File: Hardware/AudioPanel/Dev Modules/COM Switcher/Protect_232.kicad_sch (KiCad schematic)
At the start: 52 parts, among them J201 DE9_Socket_MountingHoles, J202 JST-PH UART/I2C, J203 JST-PH UART/I2C

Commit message: Small tweaks
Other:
- company: (none) -> Thomas Francois - KX∅STL
- title: (none) -> COM Port Switcher - COM Port Protection & Level Shift
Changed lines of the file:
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@@
 	(generator_version "9.0")
 	(paper "B")
+	(title_block
+		(title "COM Port Switcher - COM Port Protection & Level Shift")
+		(date "2025-07-26")
+		(rev "A")
+		(company "Thomas Francois - KX∅STL")
+	)
 	(text "RXD: Serial Data from Transceiver to Computer\n~{CTS}: Used by Transceiver to inhibit Computer from transitting serial data\nTXD: Serial Data from Computer to Transceiver\n~{RTS}: Used by Computer to inhibit Transceiver from transmitting serial data\n"
 		(exclude_from_sim no)

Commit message: Added level shifters for all SAMD21s
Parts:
- renumbered C203 to C201, C204 to C202, C208 to C203, C209 to C204, C206 to C205, C210 to C206, C201 to C207, C202 to C208, C205 to C209, C207 to C210, D204 to D201, D201 to D202, D202 to D203, D203 to D204, J203 to J201, J201 to J203, TP211 to TP202, TP202 to TP203, TP212 to TP204, TP203 to TP205, TP213 to TP206, TP204 to TP207, TP214 to TP208, TP205 to TP209, TP215 to TP210, TP206 to TP211, TP207 to TP212, TP208 to TP213, TP209 to TP214, TP210 to TP215

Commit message: Changed DB9 connectors to stacked
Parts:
- J201: renamed from J203; footprint Connector_Dsub:DSUB-9_Male_Horizontal_P2.77x2.84mm_EdgePinOffset7.70mm_Housed_MountingHolesOffset9.12mm -> Libraries:NORCOMP_189-009-513R571; symbol Connector:DE9_Socket_MountingHoles -> library_symbols:DE9_Socket_2X_Stacked; DigiKey (none) -> https://www.digikey.com/en/products/detail/norcomp-inc/189-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
- renumbered C207 to C201, C208 to C202, C201 to C203, C202 to C204, C209 to C205, C205 to C206, C210 to C207, C203 to C208, C204 to C209, C206 to C210, J201 to J203, TP203 to TP202, TP205 to TP203, TP207 to TP204, TP209 to TP205, TP211 to TP206, TP212 to TP207, TP213 to TP208, TP214 to TP209, TP215 to TP210, TP202 to TP211, TP204 to TP212, TP206 to TP213, TP208 to TP214, TP210 to TP215
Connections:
- net CTS_T: now also J201.A8; no longer J201.8
- net DCD_T: now also J201.A1; no longer J201.1
- net DSR_T: now also J201.A6; no longer J201.6
- net DTR_T: now also J201.A4; no longer J201.4
- net GND_232_FROM_RADIO: now also J201.SH1 (PAD), J201.SH2 (PAD); no longer J201.0 (PAD)
- net GND_T: now also J201.A5; no longer J201.5
- net RI_T: now also J201.A9; no longer J201.9
- net RTS_T: now also J201.A7; no longer J201.7
- net RXD_T: now also J201.A2; no longer J201.2
- net TXD_T: now also J201.A3; no longer J201.3
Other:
- moved on the sheet: J201A

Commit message: Fixed I2C pullups to 3V3
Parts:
- renumbered C203 to C201, C204 to C202, C208 to C203, C209 to C204, C206 to C205, C210 to C206, C201 to C207, C202 to C208, C205 to C209, C207 to C210, J203 to J201, J201 to J203, TP211 to TP202, TP202 to TP203, TP212 to TP204, TP203 to TP205, TP213 to TP206, TP204 to TP207, TP214 to TP208, TP205 to TP209, TP215 to TP210, TP206 to TP211, TP207 to TP212, TP208 to TP213, TP209 to TP214, TP210 to TP215
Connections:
- net CTS_232_FROM_RADIO_T renamed CTS_232_FROM_RADIO_3V3
- net CTS_T renamed CTS_3V3
- net CTS_TTL_OUT renamed CTS_3V3TL_OUT
- net DCD_T renamed DCD_3V3
- net DSR_T renamed DSR_3V3
- net DTR_T renamed DTR_3V3
- net GND_T renamed GND_3V3
- net RI_T renamed RI_3V3
- net RTS_232_TO_RADIO renamed RTS_232_3V3O_RADIO
- net RTS_232_TO_RADIO_T renamed RTS_232_3V3O_RADIO_3V3
- net RTS_T renamed RTS_3V3
- net RTS_TTL_IN renamed RTS_3V3TL_IN
- net RXD_232_FROM_RADIO_T renamed RXD_232_FROM_RADIO_3V3
- net RXD_T renamed RXD_3V3
- net RXD_TTL_OUT renamed RXD_3V3TL_OUT
- net TXD_232_TO_RADIO renamed TXD_232_3V3O_RADIO
- net TXD_232_TO_RADIO_T renamed TXD_232_3V3O_RADIO_3V3
- net TXD_T renamed TXD_3V3
- net TXD_TTL_IN renamed TXD_3V3TL_IN

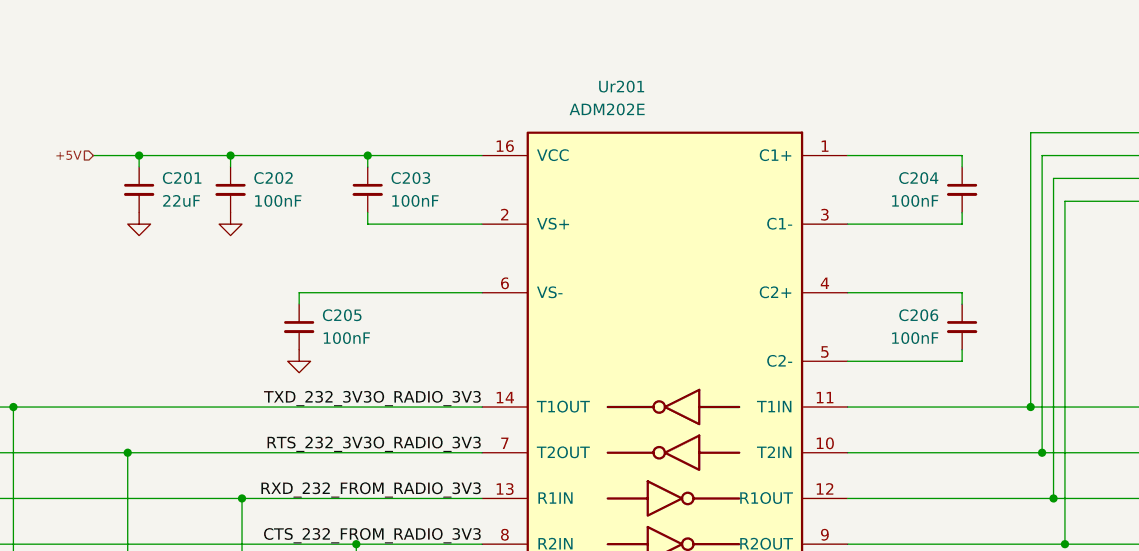
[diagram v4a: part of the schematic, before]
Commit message: Changed passives to Worthington footprints
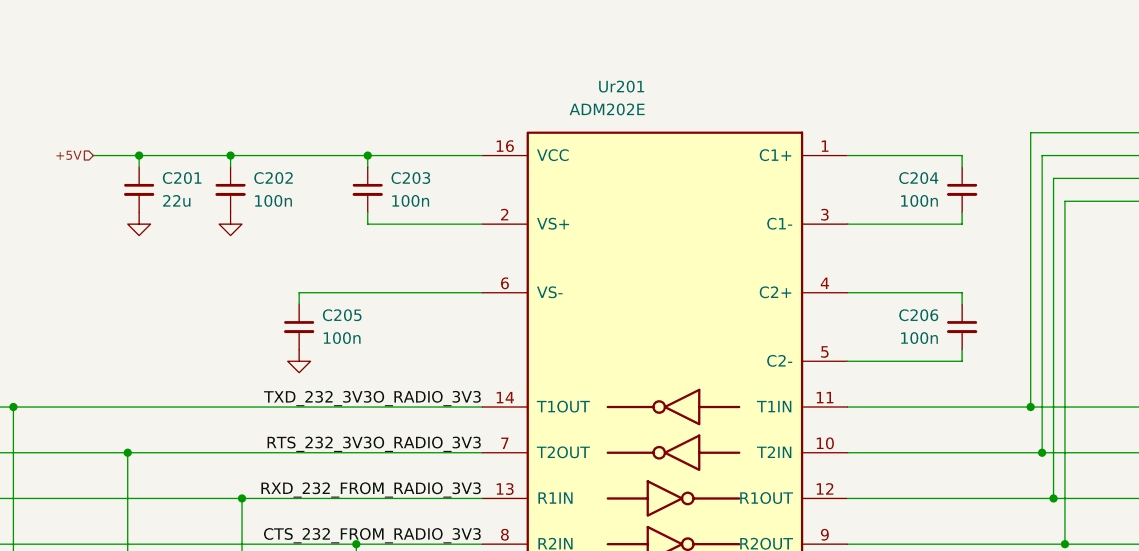
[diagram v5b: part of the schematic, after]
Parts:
- C201: value 22uF -> 22u; footprint Capacitor_SMD:C_0603_1608Metric -> Libraries:Worthington_C_0603
- C202, C203, C204, C205, C206: value 100nF -> 100n; footprint Capacitor_SMD:C_0402_1005Metric -> Libraries:Worthington_C_0402
- C207, C208, C209, C210: footprint Capacitor_SMD:C_0402_1005Metric -> Libraries:Worthington_C_0402
- L201, L202, L203, L204: footprint Inductor_SMD:L_0805_2012Metric -> Libraries:Worthington_L_0805
- R201, R202, R203, R204: footprint Resistor_SMD:R_0402_1005Metric -> Libraries:Worthington_R_0402
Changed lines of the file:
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@@
 			)
 		)
-		(property "Footprint" "Capacitor_SMD:C_0402_1005Metric"
+		(property "Footprint" "Libraries:Worthington_C_0402"
 			(at 276.86 142.24 0)
 			(effects
@@
 			)
 		)
-		(property "Footprint" "Inductor_SMD:L_0805_2012Metric"
+		(property "Footprint" "Libraries:Worthington_L_0805"
 			(at 228.6687 129.54 0)
 			(effects
@@
 			)
 		)
-		(property "Value" "22uF"
+		(property "Value" "22u"
 			(at 255.27 91.4462 0)
 			(effects
@@
 			)
 		)
-		(property "Footprint" "Capacitor_SMD:C_0603_1608Metric"
+		(property "Footprint" "Libraries:Worthington_C_0603"
 			(at 252.73 90.17 0)
 			(effects
@@
 			)
 		)
-		(property "Footprint" "Resistor_SMD:R_0402_1005Metric"
+		(property "Footprint" "Libraries:Worthington_R_0402"
 			(at 133.35 129.54 0)
 			(effects
@@
 		(lib_id "Device:C_Small")
 		(at 344.17 90.17 0)
-		(mirror y)
 		(unit 1)
 		(exclude_from_sim no)
@@
 		(on_board yes)
 		(dnp no)
-		(fields_autoplaced yes)
 		(property "Reference" "C204"
 			(at 341.63 88.9062 0)
@@
 					(size 1.27 1.27)
 				)
-				(justify left)
+				(justify right)
 			)
 		)
-		(property "Value" "100nF"
+		(property "Value" "100n"
 			(at 341.63 91.4462 0)
 			(effects
@@
 					(size 1.27 1.27)
 				)
-				(justify left)
+				(justify right)
 			)
 		)
-		(property "Footprint" "Capacitor_SMD:C_0402_1005Metric"
+		(property "Footprint" "Libraries:Worthington_C_0402"
 			(at 344.17 90.17 0)
 			(effects
@@
 			)
 		)
-		(property "Value" "100nF"
+		(property "Value" "100n"
 			(at 265.43 91.4462 0)
 			(effects
@@
 			)
 		)
-		(property "Footprint" "Capacitor_SMD:C_0402_1005Metric"
+		(property "Footprint" "Libraries:Worthington_C_0402"
 			(at 262.89 90.17 0)
 			(effects
@@
 			)
 		)
-		(property "Value" "100nF"
+		(property "Value" "100n"
 			(at 280.67 91.4462 0)
 			(effects
@@
 			)
 		)
-		(property "Footprint" "Capacitor_SMD:C_0402_1005Metric"
+		(property "Footprint" "Libraries:Worthington_C_0402"
 			(at 278.13 90.17 0)
 			(effects
@@
 			)
 		)
-		(property "Footprint" "Capacitor_SMD:C_0402_1005Metric"
+		(property "Footprint" "Libraries:Worthington_C_0402"
 			(at 264.16 142.24 0)
 			(effects
@@
 			)
 		)
-		(property "Footprint" "Capacitor_SMD:C_0402_1005Metric"
+		(property "Footprint" "Libraries:Worthington_C_0402"
 			(at 251.46 142.24 0)
 			(effects
@@
 			)
 		)
-		(property "Footprint" "Inductor_SMD:L_0805_2012Metric"
+		(property "Footprint" "Libraries:Worthington_L_0805"
 			(at 228.6 114.3 0)
 			(effects
@@
 			)
 		)
-		(property "Footprint" "Inductor_SMD:L_0805_2012Metric"
+		(property "Footprint" "Libraries:Worthington_L_0805"
 			(at 228.6 124.46 0)
 			(effects
@@
 			)
 		)
-		(property "Footprint" "Capacitor_SMD:C_0402_1005Metric"
+		(property "Footprint" "Libraries:Worthington_C_0402"
 			(at 238.76 142.24 0)
 			(effects
@@
 			)
 		)
-		(property "Footprint" "Inductor_SMD:L_0805_2012Metric"
+		(property "Footprint" "Libraries:Worthington_L_0805"
 			(at 228.6 119.38 0)
 			(effects
@@
 			)
 		)
-		(property "Footprint" "Resistor_SMD:R_0402_1005Metric"
+		(property "Footprint" "Libraries:Worthington_R_0402"
 			(at 133.35 114.3 0)
 			(effects
@@
 			)
 		)
-		(property "Footprint" "Resistor_SMD:R_0402_1005Metric"
+		(property "Footprint" "Libraries:Worthington_R_0402"
 			(at 133.35 119.38 0)
 			(effects
@@
 			)
 		)
-		(property "Value" "100nF"
+		(property "Value" "100n"
 			(at 273.05 106.6862 0)
 			(effects
@@
 			)
 		)
-		(property "Footprint" "Capacitor_SMD:C_0402_1005Metric"
+		(property "Footprint" "Libraries:Worthington_C_0402"
 			(at 270.51 105.41 0)
 			(effects
@@
 			)
 		)
-		(property "Footprint" "Resistor_SMD:R_0402_1005Metric"
+		(property "Footprint" "Libraries:Worthington_R_0402"
 			(at 133.35 124.46 0)
 			(effects
@@
 		(lib_id "Device:C_Small")
 		(at 344.17 105.41 0)
-		(mirror y)
 		(unit 1)
 		(exclude_from_sim no)
@@
 		(on_board yes)
 		(dnp no)
-		(fields_autoplaced yes)
 		(property "Reference" "C206"
 			(at 341.63 104.1462 0)
@@
 					(size 1.27 1.27)
 				)
-				(justify left)
+				(justify right)
 			)
 		)
-		(property "Value" "100nF"
+		(property "Value" "100n"
 			(at 341.63 106.6862 0)
 			(effects
@@
 					(size 1.27 1.27)
 				)
-				(justify left)
+				(justify right)
 			)
 		)
-		(property "Footprint" "Capacitor_SMD:C_0402_1005Metric"
+		(property "Footprint" "Libraries:Worthington_C_0402"
 			(at 344.17 105.41 0)
 			(effects

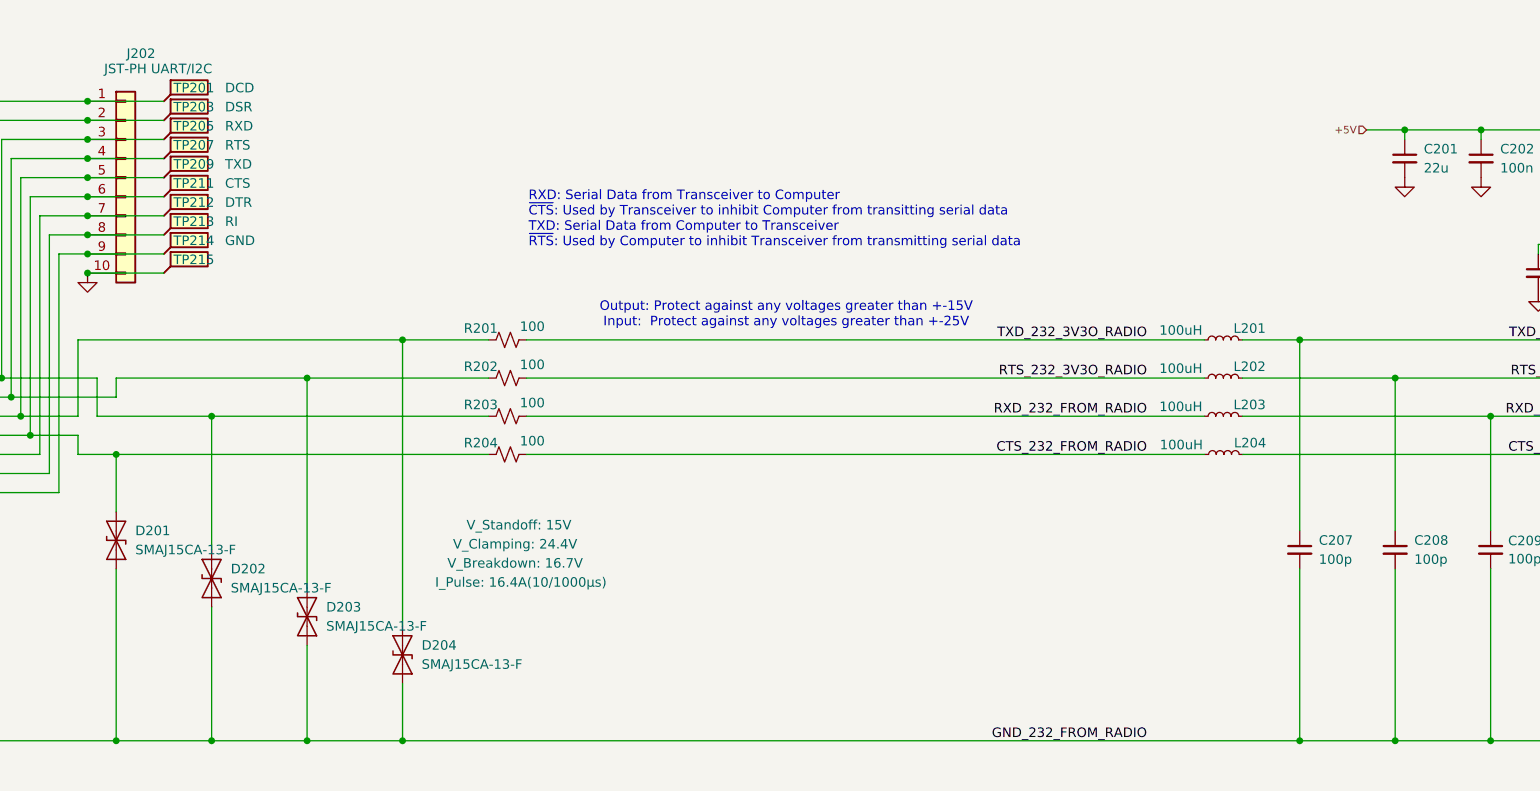
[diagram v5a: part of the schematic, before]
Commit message: Added more LEDs
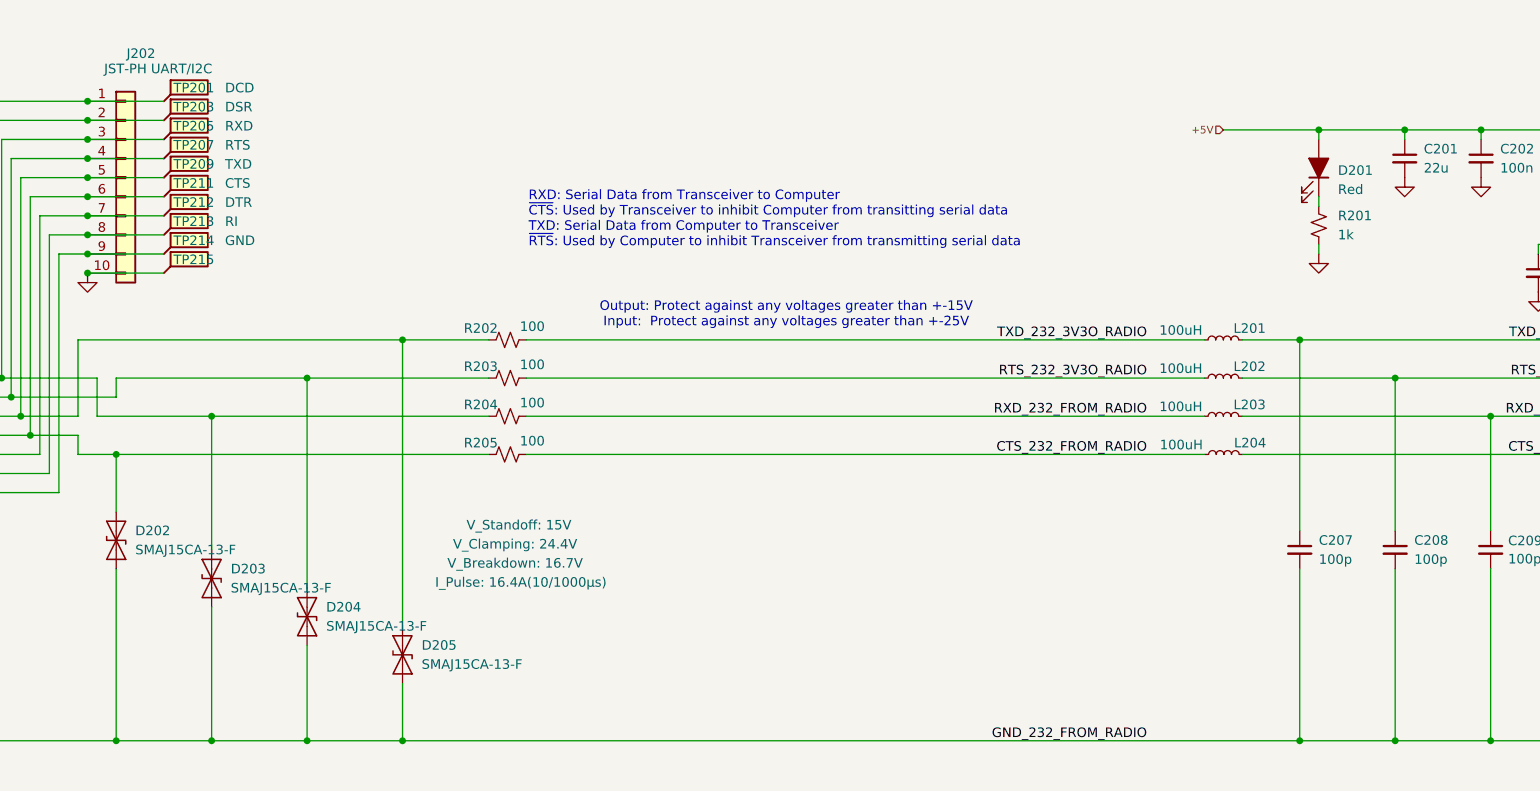
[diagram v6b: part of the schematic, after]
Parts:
- added D201: Red, LED_THT:LED_D5.0mm, symbol Device:LED_Filled
- added R201: 1k, Libraries:Worthington_R_0603, symbol Device:R_Small_US
- renumbered D201 to D202, D202 to D203, D203 to D204, D204 to D205, R201 to R202, R202 to R203, R203 to R204, R204 to R205
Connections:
- net +5V: now also D201.2 (A)
- net GND: now also R201.1
- new net: D201.1 (K), R201.2

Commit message: Resized some resistors
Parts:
- R201: footprint Libraries:Worthington_R_0603 -> Libraries:Worthington_R_0402
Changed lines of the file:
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@@
 			)
 		)
-		(property "Footprint" "Libraries:Worthington_R_0603"
+		(property "Footprint" "Libraries:Worthington_R_0402"
 			(at 241.3 99.06 0)
 			(effects

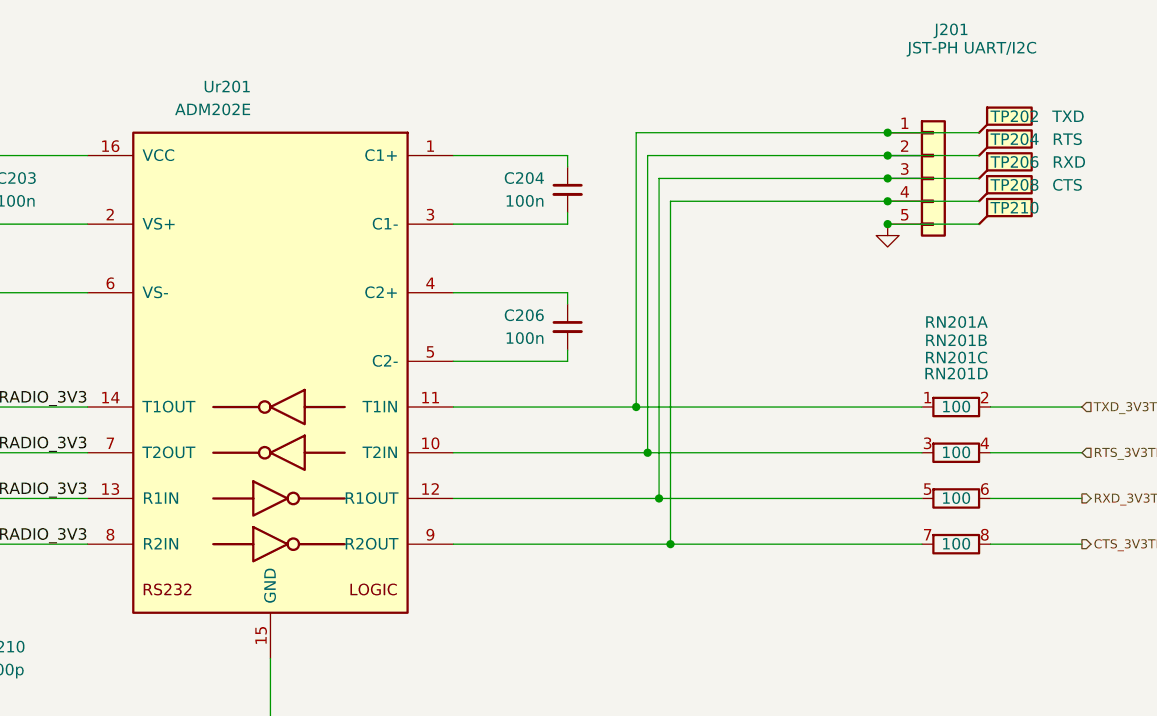
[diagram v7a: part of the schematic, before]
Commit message: Fixed footprint errors, placed onto PCBs
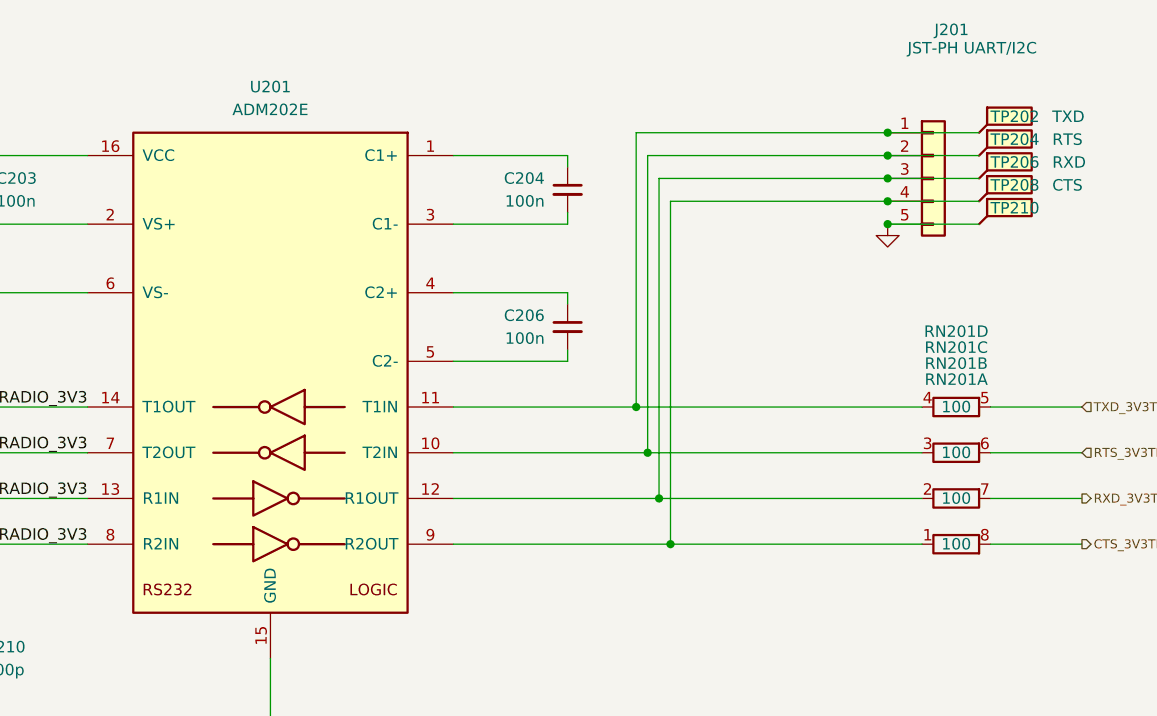
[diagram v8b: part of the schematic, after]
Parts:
- J201: footprint Connector_JST:JST_PH_S6B-PH-K_1x06_P2.00mm_Horizontal -> Connector_PinHeader_2.54mm:PinHeader_1x05_P2.54mm_Vertical
- J202: footprint Connector_JST:JST_PH_S6B-PH-K_1x06_P2.00mm_Horizontal -> Connector_PinHeader_2.54mm:PinHeader_1x10_P2.54mm_Vertical
- renumbered Ur201 to U201
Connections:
- net CTS_3V3TL_OUT: now also RN201.8; no longer RN201.8
- net RTS_3V3TL_IN: now also RN201.6; no longer RN201.4
- net RXD_3V3TL_OUT: now also RN201.7 (5); no longer RN201.6
- net TXD_3V3TL_IN: now also RN201.5; no longer RN201.2
- net at J201.2 (Pin_2), TP204.1, U201.10 (T2IN): now also RN201.3; no longer RN201.3
- net at J201.1 (Pin_1), TP202.1, U201.11 (T1IN): now also RN201.4; no longer RN201.1
- net at J201.3 (Pin_3), TP206.1, U201.12 (R1OUT): now also RN201.2; no longer RN201.5
- net at J201.4 (Pin_4), TP208.1, U201.9 (R2OUT): now also RN201.1 (4); no longer RN201.7
